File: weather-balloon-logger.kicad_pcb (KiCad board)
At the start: 2 copper layers, 80 x 78.5 mm, 27 parts, among them J1 Conn_01x02, J2 Conn_01x11, J3 SMA, J4 SMA, J5 Conn_01x02, J6 VHF, J7 HF, Q1 AO3400A, SW1 SPDT, U1 PCF8574T, U2 TC4422AVPA

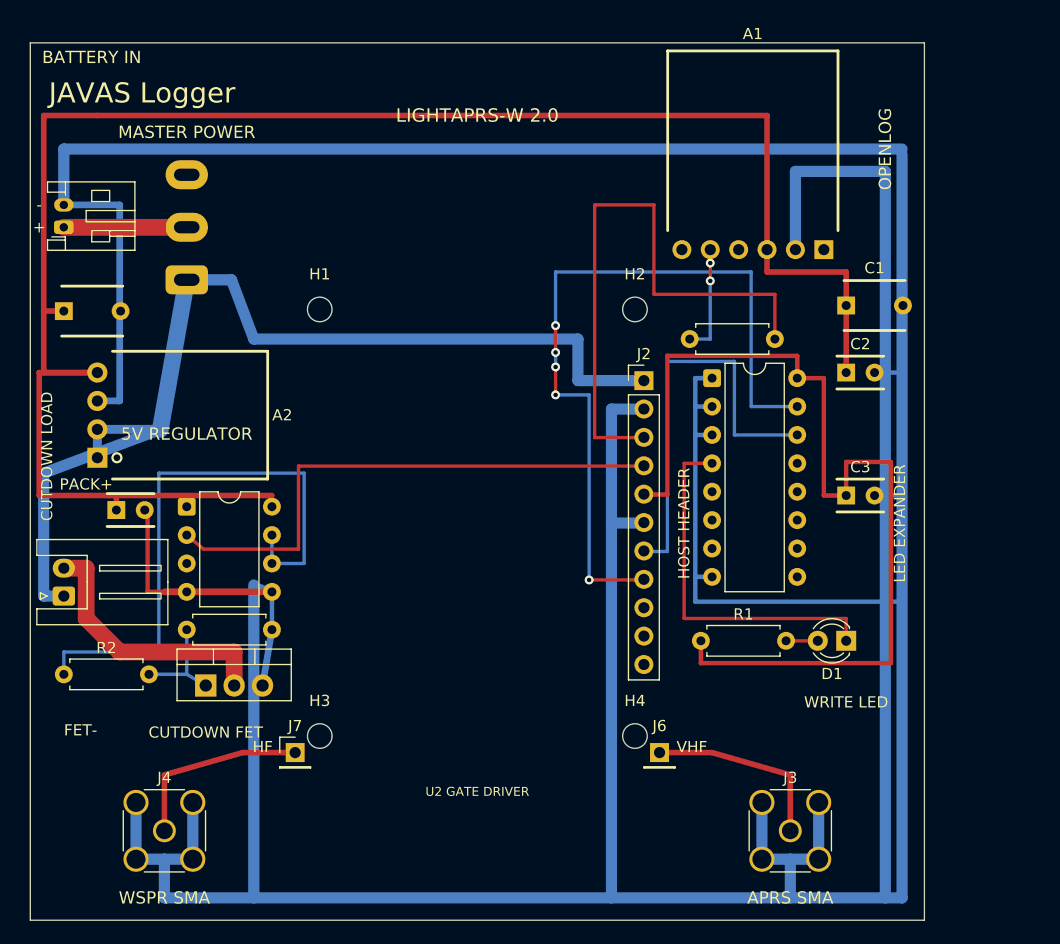
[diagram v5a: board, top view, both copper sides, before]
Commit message: fix(pcb): improve silkscreen readability
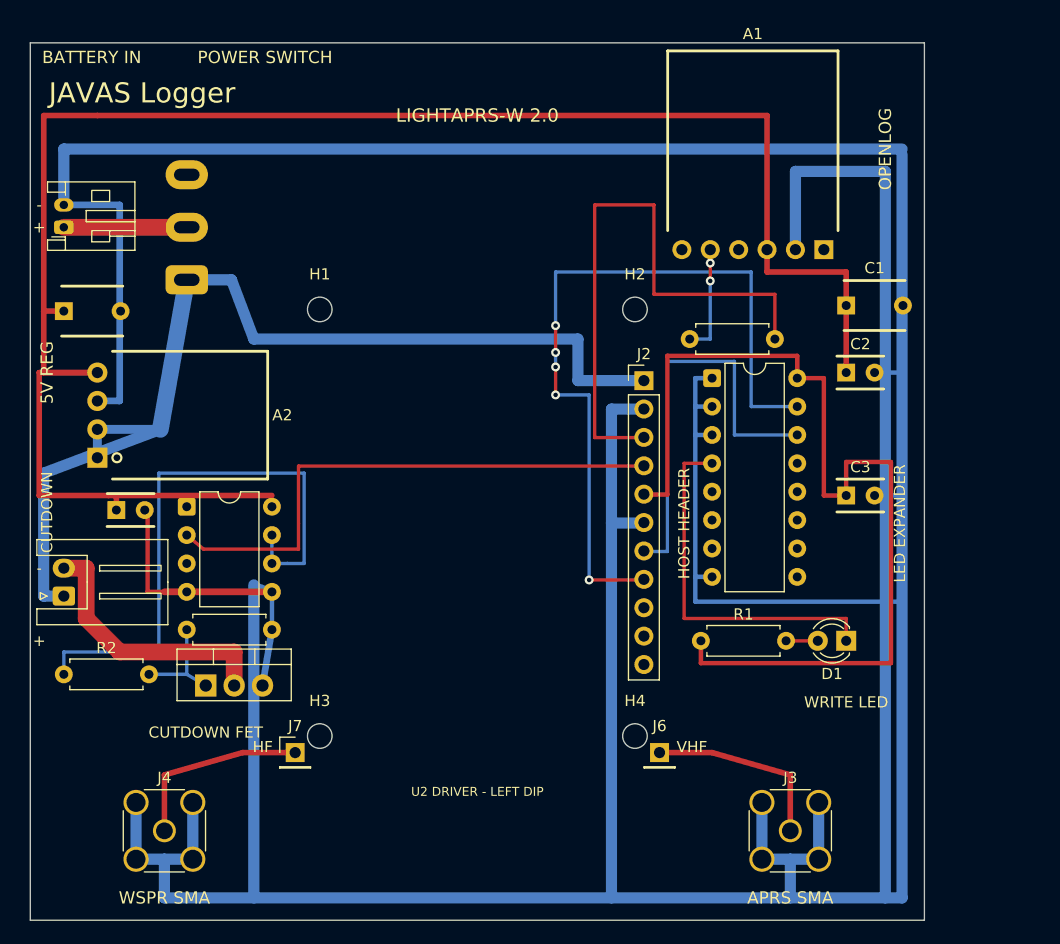
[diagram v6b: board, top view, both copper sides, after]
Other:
- board text added: "5V REG"
- board text added: "CUTDOWN"
- board text added: "POWER SWITCH"
- board text added: "U2 DRIVER - LEFT DIP"
- board text removed: "5V REGULATOR"
- board text removed: "CUTDOWN LOAD"
- board text removed: "FET-"
- board text removed: "MASTER POWER"
- board text removed: "PACK+"
- board text removed: "U2 GATE DRIVER"
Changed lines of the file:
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@@
 		(effects (font (size 1 1) (thickness 0.18)))
 	)
-	(gr_text "MASTER POWER"
-		(at 114 99.5 0)
+	(gr_text "POWER SWITCH"
+		(at 121 92.8 0)
 		(layer "F.SilkS")
 		(effects (font (size 1.1 1.1) (thickness 0.18)))
 	)
-	(gr_text "5V REGULATOR"
-		(at 114 126.5 0)
+	(gr_text "5V REG"
+		(at 101.5 121 90)
 		(layer "F.SilkS")
 		(effects (font (size 1.1 1.1) (thickness 0.18)))
@@
 		(effects (font (size 1 1) (thickness 0.18)))
 	)
-	(gr_text "U2 GATE DRIVER"
+	(gr_text "U2 DRIVER - LEFT DIP"
 		(at 140 158.5 0)
 		(layer "F.SilkS")
 		(effects (font (size 0.8 0.8) (thickness 0.15)))
 	)
-	(gr_text "CUTDOWN LOAD"
-		(at 101.5 128.5 90)
+	(gr_text "CUTDOWN"
+		(at 101.5 133.5 90)
 		(layer "F.SilkS")
 		(effects (font (size 1 1) (thickness 0.18)))
 	)
-	(gr_text "PACK+"
-		(at 105 131 0)
+	(gr_text "+"
+		(at 100.8 145 0)
 		(layer "F.SilkS")
 		(effects (font (size 1 1) (thickness 0.18)))
 	)
-	(gr_text "FET-"
-		(at 104.5 153 0)
+	(gr_text "-"
+		(at 100.8 138.5 0)
 		(layer "F.SilkS")
 		(effects (font (size 1 1) (thickness 0.18)))

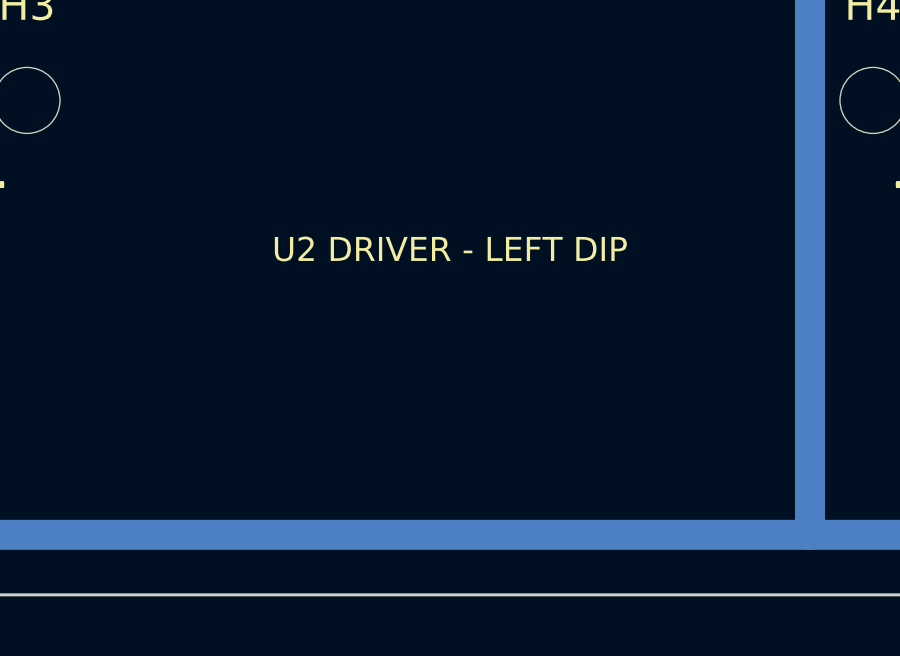
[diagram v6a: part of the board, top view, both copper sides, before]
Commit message: feat(pcb): add front silkscreen logo
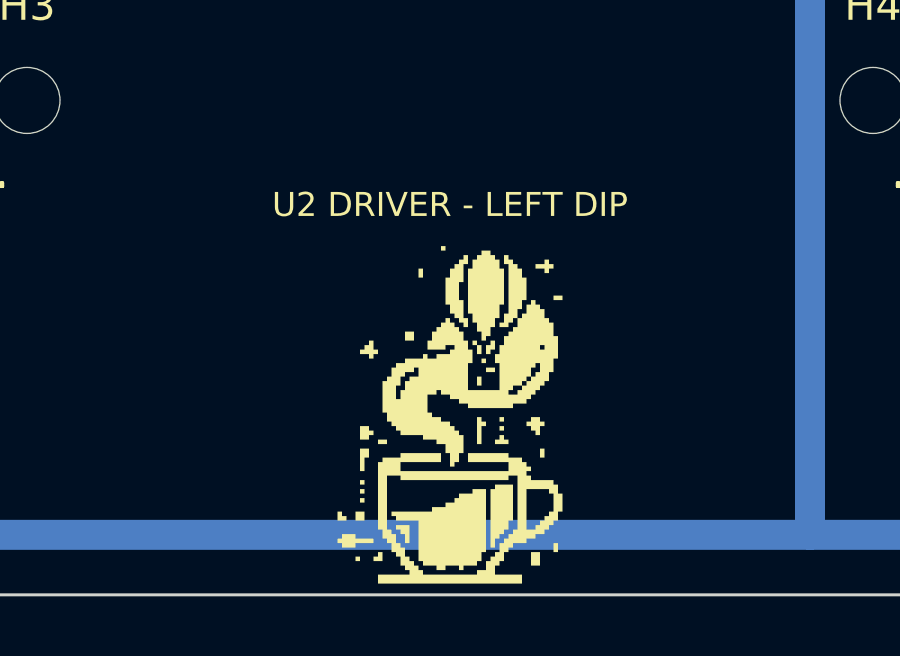
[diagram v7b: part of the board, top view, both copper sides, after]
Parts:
- added G1: Coffee Balloon Logo, CoffeeBalloon_7.5x11.25mm, F.Cu at (140.0, 164.0)

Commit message: feat(pcb): rebuild for LightHAB
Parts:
- removed C3, C4: 100nF, KEMET_C315C104K5R5TA
- removed C5: 4.7uF, KEMET_C322C475K5R5TA
- removed J4: SMA, SMA_Amphenol_132134_Vertical
- removed J6: VHF, PinHeader_1x01_P2.54mm_Vertical
- removed J7: HF, PinHeader_1x01_P2.54mm_Vertical
- removed Q1: AO3400A, TO-220-3_Vertical
- removed R3: 1M, R_Axial_DIN0207_L6.3mm_D2.5mm_P7.62mm_Horizontal
- removed SW1: SPDT, SW_CK_7101SYZQE
- removed U1: PCF8574T, DIP-16_W7.62mm
- removed U2: TC4422AVPA, DIP-8_W7.62mm
- D1: value LTST-C190KGKT -> WP710A10SGC
- G1: value Coffee Balloon Logo -> Coffee Balloon
- H1, H2, H3, H4: value M2_STANDOFF -> LIGHTHAB HOLE - UNVERIFIED; footprint MountingHole_2.2mm_M2 -> MountingHole_3.2mm_M3
- J1: value Conn_01x02 -> LightHAB VBATT/GND; footprint JST_PH_S2B-PH-K_1x02_P2.00mm_Horizontal -> PinHeader_1x02_P2.54mm_Vertical
- J2: value Conn_01x11 -> LightHABTracker 1.0; footprint PinHeader_1x11_P2.54mm_Vertical -> PinHeader_1x09_P2.54mm_Vertical
- J3: value SMA -> LightHAB OUT1/GND; footprint SMA_Amphenol_132134_Vertical -> PinHeader_1x02_P2.54mm_Vertical
- J5: value Conn_01x02 -> Cutdown output
- R2: value 100R -> 100k
- moved C1 59.5 mm to (116.0, 132.0)
- moved C2 59.5 mm to (116.0, 138.0)
- moved D1 58.1 mm to (122.7, 116.0)
- moved R1 57.8 mm to (110.0, 116.0)
- moved A1 54.5 mm to (116.5, 110.0)
- moved J1 53.3 mm to (144.0, 142.0), turned to 0 degrees
- moved R4 40.4 mm to (128.0, 106.0)
- moved H2 35.8 mm to (186.0, 99.0)
- moved H4 34.3 mm to (186.0, 166.0)
- moved R2 28.9 mm to (110.0, 120.0)
- moved J3 25.0 mm to (144.0, 155.0)
- moved J2 22.4 mm to (136.5, 109.0)
- moved H1 20.3 mm to (138.0, 99.0)
- moved A2 19.2 mm to (103.0, 140.0), turned to 0 degrees
- moved J5 17.9 mm to (108.5, 158.0), turned to 180 degrees
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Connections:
- A2 pad 1: PACK_SW -> VBATT
- A2 pad 2: PACK_SW -> VBATT
- J1 pad 1: PACK_IN -> VBATT
- J2 pad 1: PACK_SW -> UART_TX
- J2 pad 2: GND -> LED_N
- J2 pad 3: UART_TX -> 3V3
- J2 pad 4: CUTDOWN_CTRL -> GND
- J2 pad 5: 3V3 -> (no net)
- J2 pad 6: GND -> (no net)
- J2 pad 7: I2C_SCL -> (no net)
- J2 pad 8: I2C_SDA -> (no net)
- J3 pad 1: RF_APRS -> OUT1
- J5 pad 1: PACK_SW -> OUT1
- J5 pad 2: CUTDOWN_DRAIN -> GND
- R2 pad 1: CUTDOWN_DRIVE -> 3V3
- R2 pad 2: CUTDOWN_GATE -> LED_N
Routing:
- net GND: track 512.5 -> 182.4 mm
- net PACK_SW: track 94.0 -> 0.00 mm
- net LOGGER_5V: track 162.7 -> 70.4 mm
- net I2C_SDA: track 69.1 -> 0.00 mm, vias 5 -> 0
- net CUTDOWN_DRIVE: track 53.0 -> 0.00 mm
- net CUTDOWN_CTRL: track 48.8 -> 0.00 mm
- net VBATT: track 0.00 -> 43.9 mm
- net UART_TX: track 53.3 -> 11.5 mm
- net 3V3: track 87.0 -> 46.4 mm
- net OUT1: track 0.00 -> 38.5 mm
- net I2C_SCL: track 37.3 -> 0.00 mm
- net CUTDOWN_DRAIN: track 24.0 -> 0.00 mm
- net RF_WSPR: track 17.0 -> 0.00 mm
- net RF_APRS: track 17.0 -> 0.00 mm
- net PACK_IN: track 11.0 -> 0.00 mm
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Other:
- board size 80 x 78.5 mm -> 90 x 80 mm
- board text added: "1 OUT1 2 GND"
- board text added: "ACTIVITY"
- board text added: "COMPONENTS OUT / 18-20mm STACK"
- board text added: "LIGHTHAB 56x75 PHOTO-DERIVED ZONE"
- board text added: "LIGHTHAB EXTENDED PINS 1=A1"
- board text added: "LOGGER 5V"
- board text added: "OUT1 / GND"
- board text added: "SMA KEEP-OUT"
- board text added: "UNVERIFIED LIGHTHAB FIT - DO NOT FABRICATE"
- board text added: "USB KEEP-OUT"
- board text added: "VBATT / GND"
- board text added: "microSD ACCESS"
- board text removed: "+"
- board text removed: "-"
- board text removed: "5V REG"
- board text removed: "APRS 5mm RF CLEARANCE"
- board text removed: "APRS SMA"
- board text removed: "BATTERY IN"
- board text removed: "CUTDOWN FET"
- board text removed: "HF"
- board text removed: "HOST HEADER"
- board text removed: "JAVAS Logger"
- board text removed: "LED EXPANDER"
- board text removed: "LIGHTAPRS-W 2.0"
- board text removed: "LIGHTAPRS-W 2.0 FACE-UP ZONE 32.77 x 54.80 mm"
- board text removed: "POWER SWITCH"
- board text removed: "RESERVED ESD"
- board text removed: "U2 DRIVER - LEFT DIP"
- board text removed: "VHF"
- board text removed: "WRITE LED"
- board text removed: "WSPR 5mm RF CLEARANCE"
- board text removed: "WSPR SMA"
